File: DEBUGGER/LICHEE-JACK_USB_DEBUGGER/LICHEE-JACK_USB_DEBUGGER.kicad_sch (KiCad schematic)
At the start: 47 parts, among them Q1 AO3401A, U1 USB2422/MJ, U3 TPSPX3819M5-L-3-3, U4 CP2102-GMR, X1 XL7EL89CMI-111YLC-24M

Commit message: replace some obj
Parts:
- removed LED3: LED_ORANGE/YELLOW_TXD, YLED0603O:LED0603-FD, symbol YLED0603O:YLED0603O
- added LED5: LED_YELLOW_RXD, YLED0603G:LED0603-FD, symbol YLED0603G:YLED0603G
- added TP4: TP_VBUS, TestPoint:TestPoint_Pad_D1.0mm, symbol Connector:TestPoint
- added TP5: TP_GND, TestPoint:TestPoint_Pad_D1.0mm, symbol Connector:TestPoint
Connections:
- net GNDREF: now also TP5.1
- net TXD: now also LED5.1 (+)
- net VBUS: now also TP4.1
- net at R10.1: now also LED5.2 (-)
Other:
- moved on the sheet: TP1, TP2, TP3

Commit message: update some info
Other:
- company: KaliAssistant -> KaliAssistant <work.kaliassistant.github@gmail.com>
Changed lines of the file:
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@@
 	(title_block
 		(title "Lichee-Jack USB Debugger")
-		(date "2026-01-11")
+		(date "2026-01-13")
 		(rev "1.0")
-		(company "KaliAssistant")
+		(company "KaliAssistant <work.kaliassistant.github@gmail.com>")
 	)
 	(rectangle

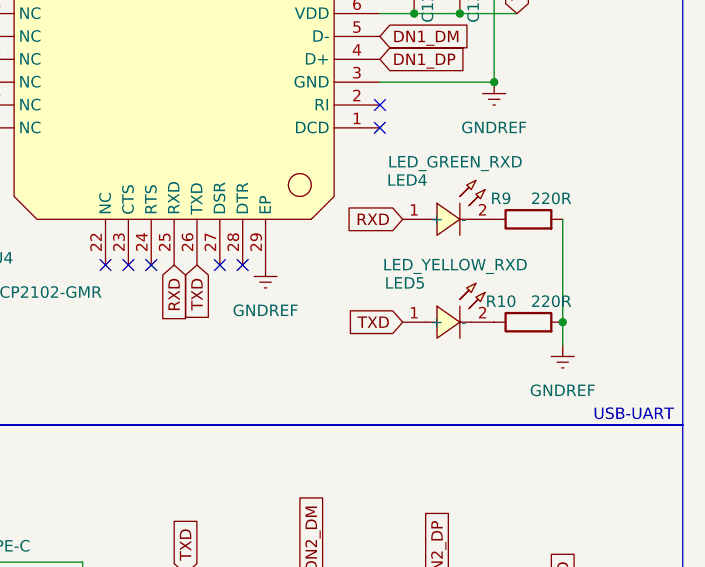
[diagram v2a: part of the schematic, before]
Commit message: rename LED5
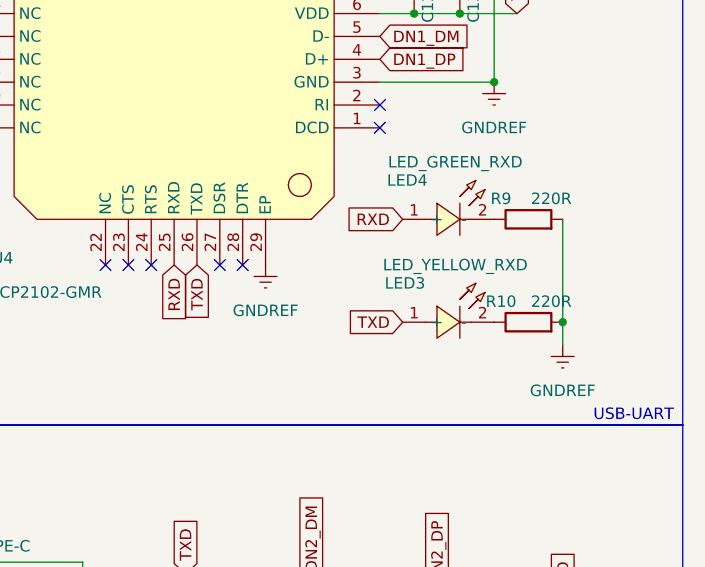
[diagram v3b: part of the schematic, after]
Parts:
- renumbered LED5 to LED3
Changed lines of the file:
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@@
 		(on_board yes)
 		(dnp no)
-		(property "Reference" "LED5"
+		(property "Reference" "LED3"
 			(at 254.254 70.612 0)
 			(effects
@@
 			(project "LICHEE-JACK_USB_DEBUGGER"
 				(path "/307002bb-0079-42fe-bf10-05ee883dca50"
-					(reference "LED5")
+					(reference "LED3")
 					(unit 1)
 				)

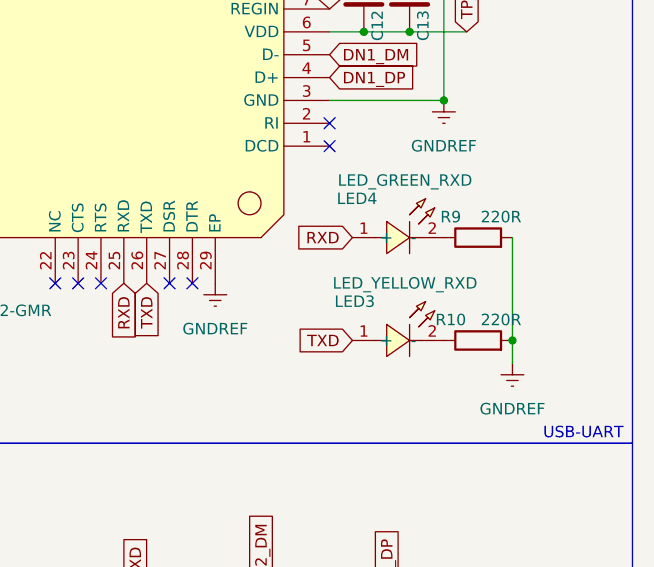
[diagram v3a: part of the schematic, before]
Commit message: rename LED3
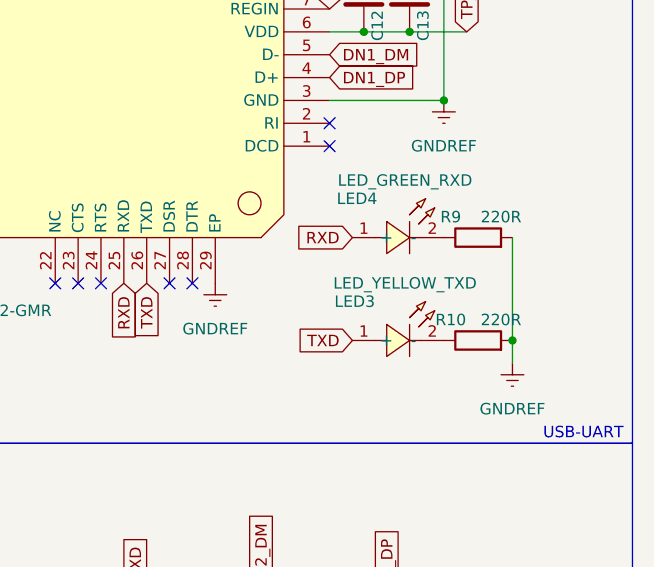
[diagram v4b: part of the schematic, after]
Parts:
- LED3: value LED_YELLOW_RXD -> LED_YELLOW_TXD
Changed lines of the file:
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@@
 			)
 		)
-		(property "Value" "LED_YELLOW_RXD"
+		(property "Value" "LED_YELLOW_TXD"
 			(at 259.84 68.58 0)
 			(effects

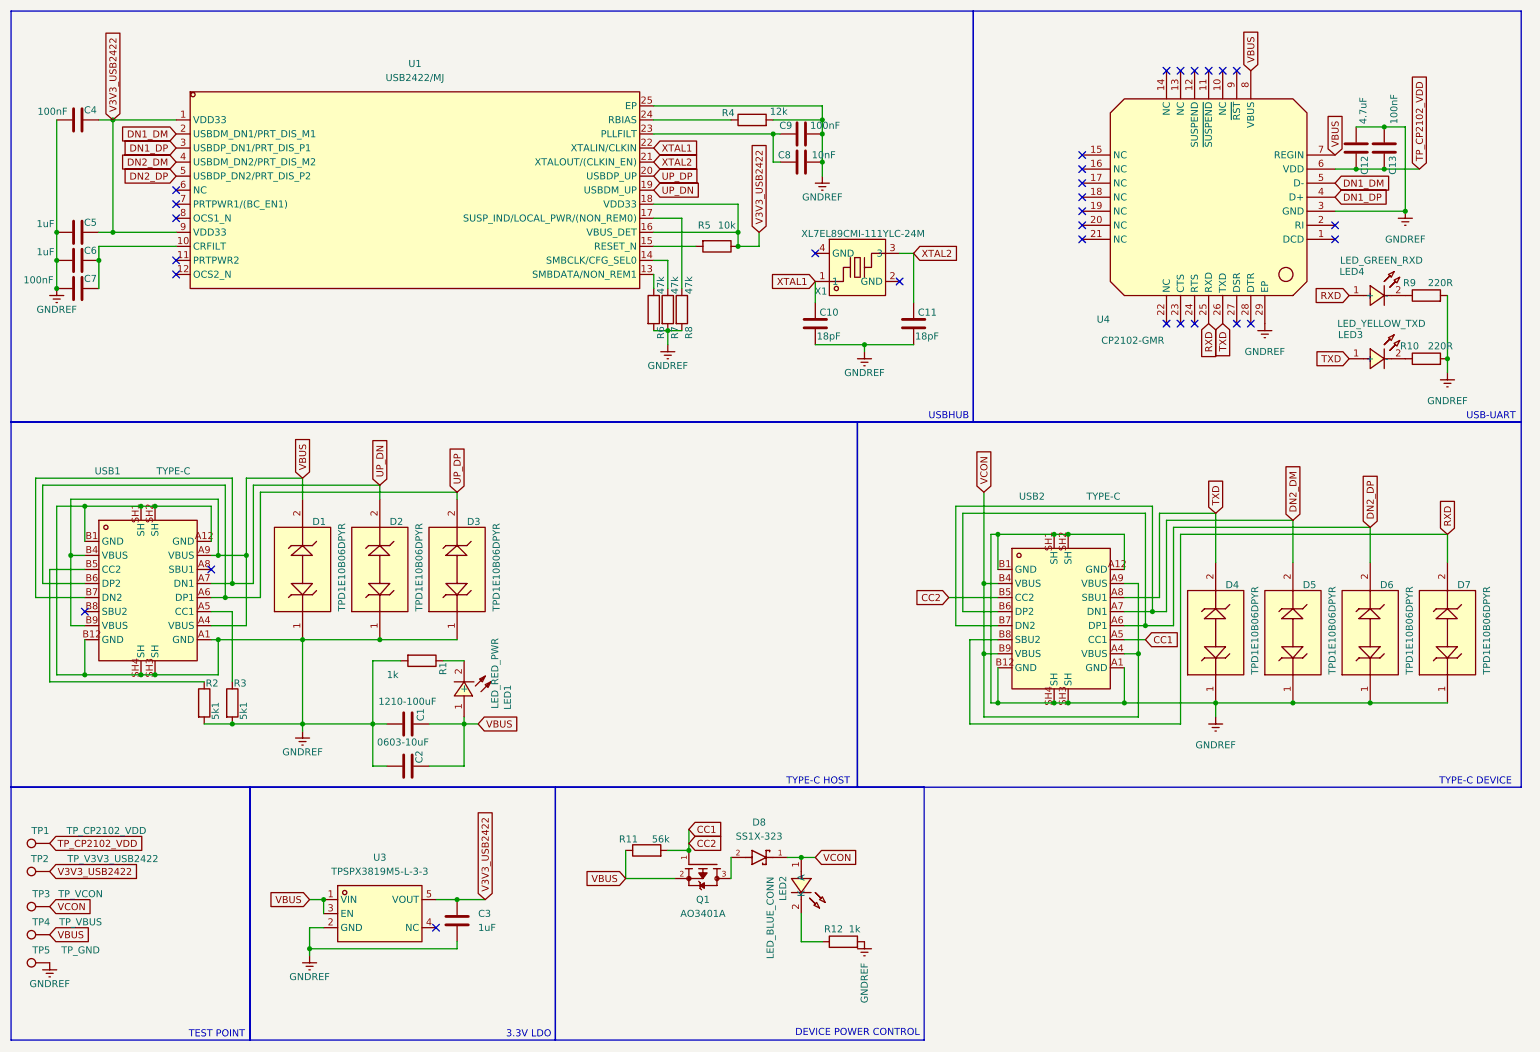
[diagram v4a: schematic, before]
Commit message: fix TX/RX LED, USB DEBUGGER v1.1
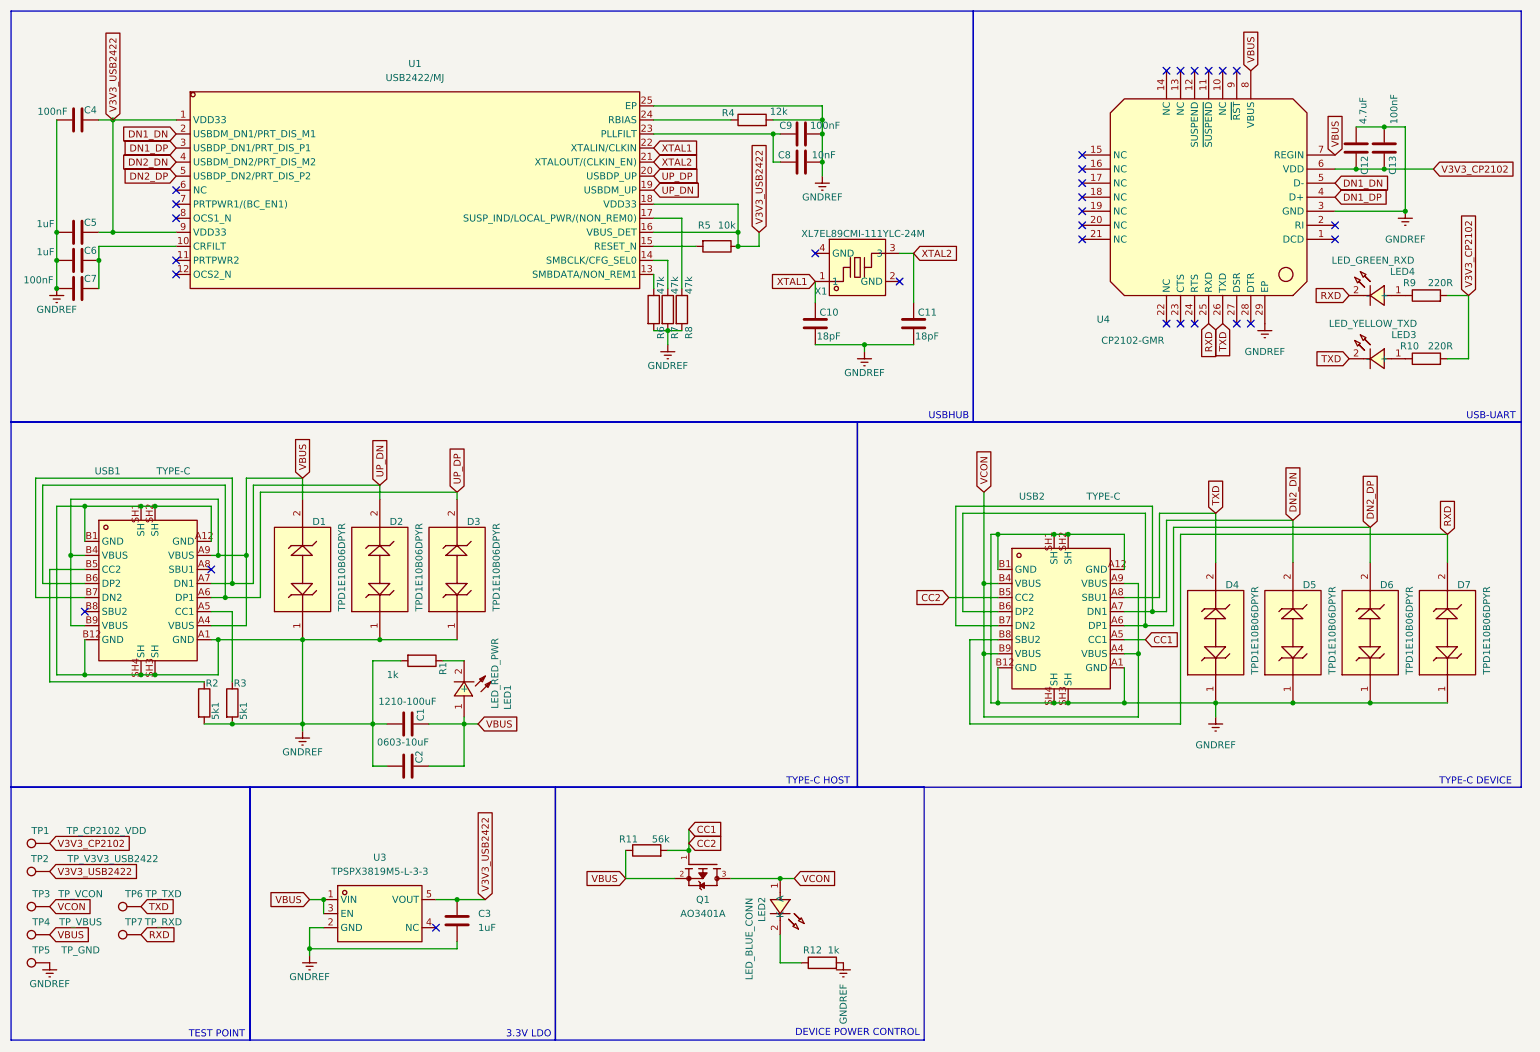
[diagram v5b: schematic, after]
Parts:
- removed D8: SS1X-323, PMEG4010CEJ_115:DIO_PMEG4010CEJ_115, symbol PMEG4010CEJ_115:PMEG4010CEJ_115
- added TP6: TP_TXD, TestPoint:TestPoint_Pad_D1.0mm, symbol Connector:TestPoint
- added TP7: TP_RXD, TestPoint:TestPoint_Pad_D1.0mm, symbol Connector:TestPoint
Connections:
- net GNDREF: no longer R10.2, R9.2
- net RXD: now also LED4.2 (-), TP7.1; no longer LED4.1 (+)
- net TXD: now also LED3.2 (-), TP6.1; no longer LED3.1 (+)
- net VCON: now also Q1.3
- net at R10.1: now also LED3.1 (+); no longer LED3.2 (-)
- net at R9.1: now also LED4.1 (+); no longer LED4.2 (-)
- net DN1_DM renamed DN1_DN
- net DN2_DM renamed DN2_DN
- net TP_CP2102_VDD renamed V3V3_CP2102
- net V3V3_CP2102: now also R10.2, R9.2
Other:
- moved on the sheet: LED2, R12
